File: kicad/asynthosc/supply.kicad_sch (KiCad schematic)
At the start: 52 parts, among them J1 USB_B_Micro, J17 Conn_01x02, J2 Conn_02x05_Odd_Even, U1 LM1117S-3.3, U2 LMR62421XMF, U3 USBLC6-2SC6, U4 LM1117S-5.0, U5 Si1869DH

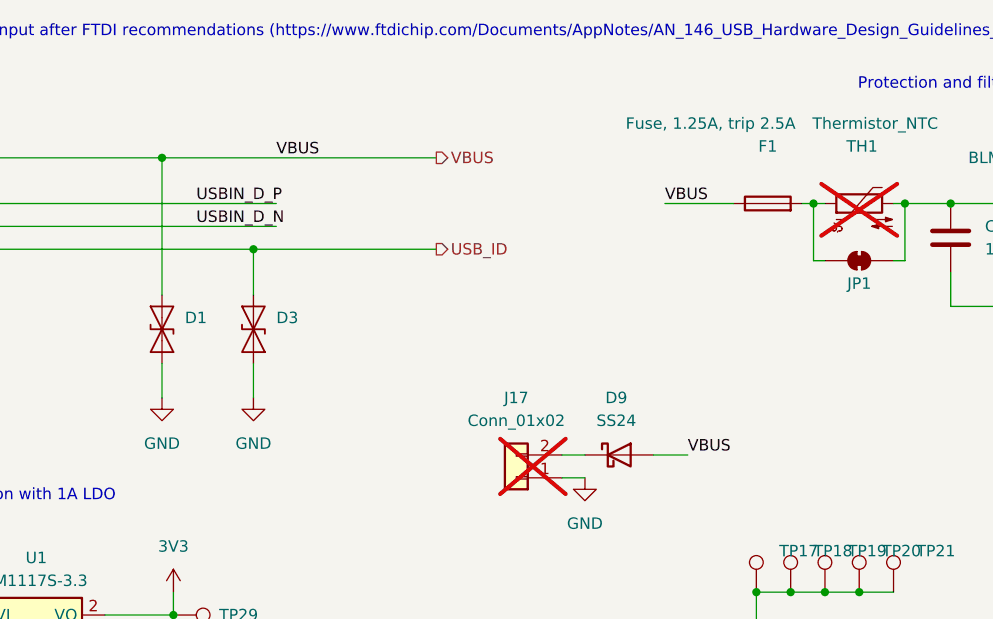
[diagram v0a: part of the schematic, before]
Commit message: fix: put all components after fuse
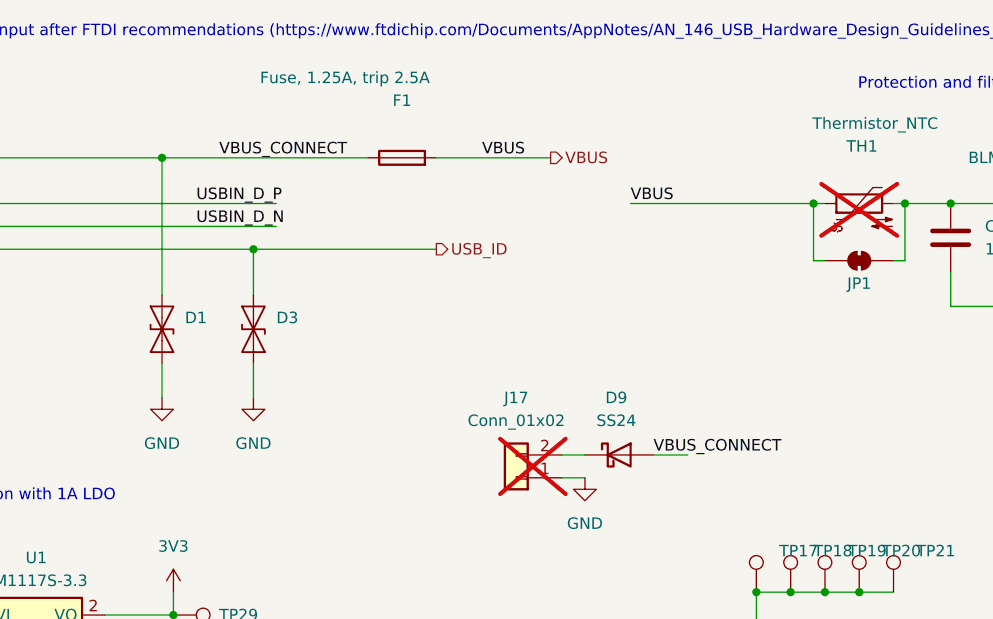
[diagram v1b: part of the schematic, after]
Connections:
- net VBUS: now also F1.2, JP1.1 (A), TH1.1; no longer D1.2 (A2), D9.2 (A), F1.1, J1.1 (VBUS)
- new net VBUS_CONNECT: D1.2 (A2), D9.2 (A), F1.1, J1.1 (VBUS)
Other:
- moved on the sheet: F1
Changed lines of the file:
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@@
 	(wire
 		(pts
-			(xy 123.19 43.18) (xy 130.81 43.18)
+			(xy 119.38 43.18) (xy 139.7 43.18)
 		)
 		(stroke
@@
 	(wire
 		(pts
-			(xy 67.31 38.1) (xy 97.79 38.1)
+			(xy 67.31 38.1) (xy 90.17 38.1)
 		)
 		(stroke
@@
 	(wire
 		(pts
+			(xy 97.79 38.1) (xy 110.49 38.1)
+		)
+		(stroke
+			(width 0)
+			(type default)
+		)
+	)
+	(wire
+		(pts
 			(xy 139.7 43.18) (xy 140.97 43.18)
 		)
@@
 	(wire
 		(pts
-			(xy 138.43 43.18) (xy 139.7 43.18)
-		)
-		(stroke
-			(width 0)
-			(type default)
-		)
-	)
-	(wire
-		(pts
 			(xy 69.85 193.04) (xy 69.85 203.2)
 		)
@@
 	)
 	(label "VBUS"
-		(at 125.73 71.12 0)
+		(at 29.21 177.8 0)
 		(fields_autoplaced yes)
 		(effects
@@
 		)
 	)
-	(label "VBUS"
-		(at 29.21 177.8 0)
+	(label "VBUS_CONNECT"
+		(at 73.66 38.1 0)
 		(fields_autoplaced yes)
 		(effects
@@
 		)
 	)
+	(label "VBUS_CONNECT"
+		(at 121.92 71.12 0)
+		(fields_autoplaced yes)
+		(effects
+			(font
+				(size 1.27 1.27)
+			)
+			(justify left bottom)
+		)
+	)
 	(label "5V_EUR"
 		(at 120.65 248.92 0)
@@
 	)
 	(label "VBUS"
-		(at 123.19 43.18 0)
+		(at 119.38 43.18 0)
 		(fields_autoplaced yes)
 		(effects
@@
 	)
 	(label "VBUS"
-		(at 80.01 38.1 0)
+		(at 102.87 38.1 0)
 		(fields_autoplaced yes)
 		(effects
@@
 	(hierarchical_label "VBUS"
 		(shape output)
-		(at 97.79 38.1 0)
+		(at 110.49 38.1 0)
 		(fields_autoplaced yes)
 		(effects
@@
 	(symbol
 		(lib_id "Device:Fuse")
-		(at 134.62 43.18 90)
+		(at 93.98 38.1 90)
 		(unit 1)
 		(exclude_from_sim yes)
@@
 		(dnp no)
 		(property "Reference" "F1"
-			(at 134.62 36.83 90)
+			(at 93.98 31.75 90)
 			(effects
 				(font
@@
 		)
 		(property "Value" "Fuse, 1.25A, trip 2.5A"
-			(at 128.27 34.29 90)
+			(at 87.63 29.21 90)
 			(effects
 				(font
@@
 		)
 		(property "Footprint" "Resistor_SMD:R_0805_2012Metric"
-			(at 134.62 44.958 90)
+			(at 93.98 39.878 90)
 			(effects
 				(font
@@
 		)
 		(property "Datasheet" "~"
-			(at 134.62 43.18 0)
+			(at 93.98 38.1 0)
 			(effects
 				(font
@@
 		)
 		(property "Description" "Fuse"
-			(at 134.62 43.18 0)
+			(at 93.98 38.1 0)
 			(effects
 				(font
@@
 		)
 		(property "RefNum" "_generic_"
-			(at 134.62 43.18 90)
+			(at 93.98 38.1 90)
 			(effects
 				(font
@@
 		)
 		(property "LCSC" ""
-			(at 134.62 43.18 0)
+			(at 93.98 38.1 0)
 			(effects
 				(font
@@
 		)
 		(property "Manufacturer" ""
-			(at 134.62 43.18 0)
+			(at 93.98 38.1 0)
 			(effects
 				(font
@@
 		)
 		(property "JLC" "0805"
-			(at 134.62 43.18 0)
+			(at 93.98 38.1 0)
 			(effects
 				(font

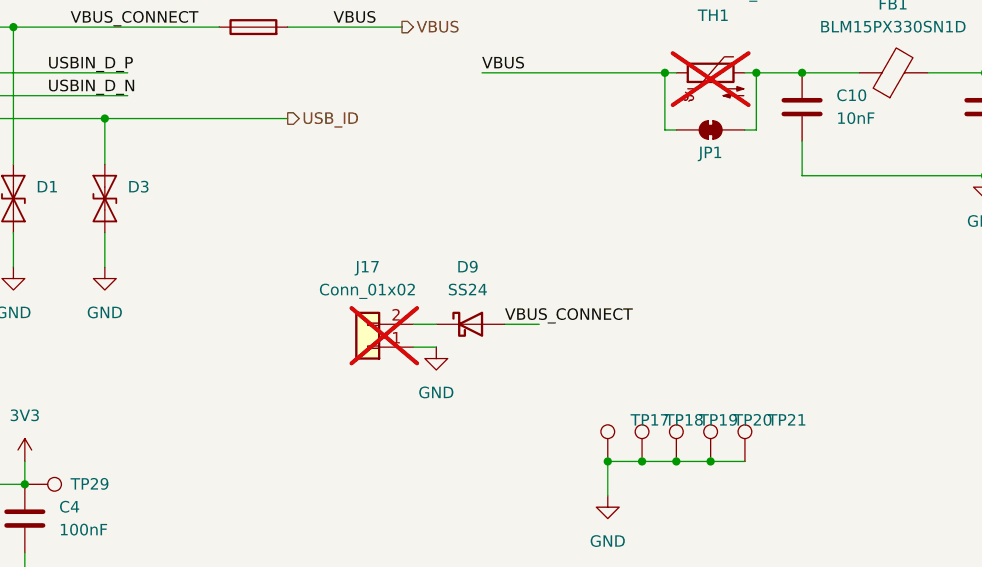
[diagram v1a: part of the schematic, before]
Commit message: fix: divider bridge stupid mistake
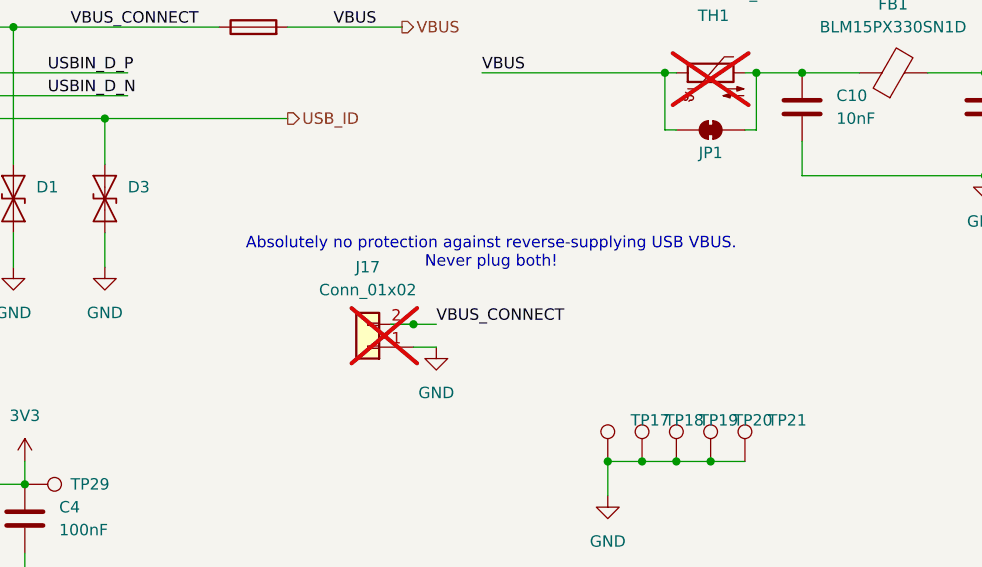
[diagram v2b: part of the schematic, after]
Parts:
- removed D9: SS24, Diode_SMD:D_SMA, symbol Diode:SS24
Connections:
- net VBUS_CONNECT: now also J17.2 (Pin_2)
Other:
- note added: "Absolutely no protection against reverse-supplying USB VBUS. Never plug both!"
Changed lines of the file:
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@@
 	)
 	(junction
+		(at 111.76 71.12)
+		(diameter 0)
+		(color 0 0 0 0)
+	)
+	(junction
 		(at 91.44 193.04)
 		(diameter 0)
@@
 	(wire
 		(pts
-			(xy 111.76 71.12) (xy 114.3 71.12)
+			(xy 109.22 71.12) (xy 111.76 71.12)
 		)
 		(stroke
@@
 	(wire
 		(pts
-			(xy 125.73 71.12) (xy 121.92 71.12)
-		)
-		(stroke
-			(width 0)
-			(type default)
-		)
-	)
-	(wire
-		(pts
 			(xy 91.44 203.2) (xy 91.44 209.55)
 		)
@@
 	(wire
 		(pts
+			(xy 111.76 71.12) (xy 114.3 71.12)
+		)
+		(stroke
+			(width 0)
+			(type default)
+		)
+	)
+	(wire
+		(pts
 			(xy 52.07 187.96) (xy 46.99 187.96)
 		)
@@
 		)
 	)
+	(text "Absolutely no protection against reverse-supplying USB VBUS.\nNever plug both!"
+		(exclude_from_sim no)
+		(at 120.396 63.246 0)
+		(effects
+			(font
+				(size 1.27 1.27)
+			)
+		)
+	)
 	(text "Display supply for standalone Eurorack"
 		(exclude_from_sim no)
@@
 	)
 	(label "VBUS_CONNECT"
-		(at 121.92 71.12 0)
+		(at 114.3 71.12 0)
 		(fields_autoplaced yes)
 		(effects
@@
 					(unit 1)
 				)
-			)
-		)
-	)
-	(symbol
-		(lib_id "Diode:SS24")
-		(at 118.11 71.12 0)
-		(unit 1)
-		(exclude_from_sim no)
-		(in_bom yes)
-		(on_board yes)
-		(dnp no)
-		(fields_autoplaced yes)
-		(property "Reference" "D9"
-			(at 117.7925 64.77 0)
-			(effects
-				(font
-					(size 1.27 1.27)
-				)
-			)
-		)
-		(property "Value" "SS24"
-			(at 117.7925 67.31 0)
-			(effects
-				(font
-					(size 1.27 1.27)
-				)
-			)
-		)
-		(property "Footprint" "Diode_SMD:D_SMA"
-			(at 118.11 75.565 0)
-			(effects
-				(font
-					(size 1.27 1.27)
-				)
-				(hide yes)
-			)
-		)
-		(property "Datasheet" "https://www.vishay.com/docs/88748/ss22.pdf"
-			(at 118.11 71.12 0)
-			(effects
-				(font
-					(size 1.27 1.27)
-				)
-				(hide yes)
-			)
-		)
-		(property "Description" "40V 2A Schottky Diode, SMA"
-			(at 118.11 71.12 0)
-			(effects
-				(font
-					(size 1.27 1.27)
-				)
-				(hide yes)
-			)
-		)
-		(property "LCSC" "C3014007"
-			(at 118.11 71.12 0)
-			(effects
-				(font
-					(size 1.27 1.27)
-				)
-				(hide yes)
-			)
-		)
-		(property "Manufacturer" "Fosan"
-			(at 118.11 71.12 0)
-			(effects
-				(font
-					(size 1.27 1.27)
-				)
-				(hide yes)
-			)
-		)
-		(property "RefNum" "SS24"
-			(at 118.11 71.12 0)
-			(effects
-				(font
-					(size 1.27 1.27)
-				)
-				(hide yes)
-			)
-		)
-		(property "JLC" "SMA"
-			(at 118.11 71.12 0)
-			(effects
-				(font
-					(size 1.27 1.27)
-				)
-				(hide yes)
-			)
-		)
-		(pin "1"
-		)
-		(pin "2"
-		)
-		(instances
-			(project "asynthosc"
-				(path "/d73e377a-a016-415f-8824-91cc6e4907b9/22ca5166-338c-4a24-8f8a-545e4a0286bf"
-					(reference "D9")
-					(unit 1)
-				)

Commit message: fix: ldo tab is vout
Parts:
- U1, U4: footprint Package_TO_SOT_SMD:SOT-223 -> Package_TO_SOT_SMD:SOT-223-3_TabPin2
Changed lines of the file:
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@@
 			)
 		)
-		(property "Footprint" "Package_TO_SOT_SMD:SOT-223"
+		(property "Footprint" "Package_TO_SOT_SMD:SOT-223-3_TabPin2"
 			(at 105.41 255.27 0)
 			(effects
@@
 			)
 		)
-		(property "Footprint" "Package_TO_SOT_SMD:SOT-223"
+		(property "Footprint" "Package_TO_SOT_SMD:SOT-223-3_TabPin2"
 			(at 53.34 88.9 0)
 			(effects

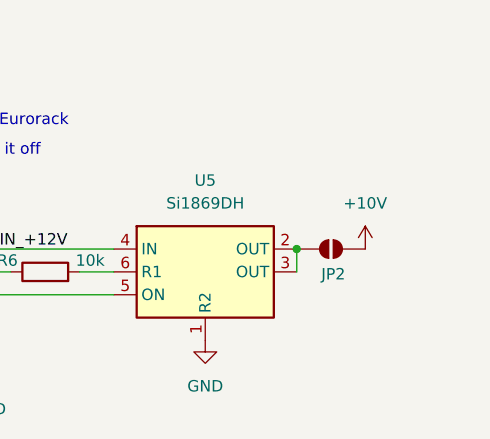
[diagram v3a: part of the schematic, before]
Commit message: sch: add decoupling capacitor to 10V switch
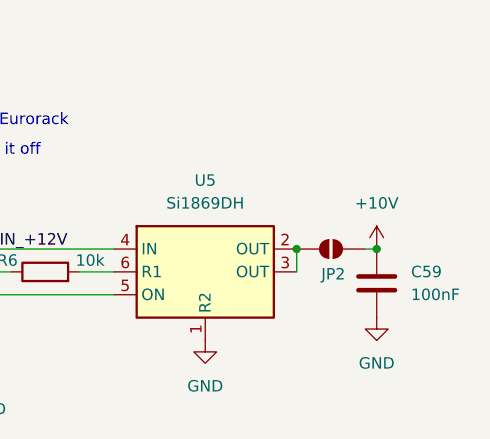
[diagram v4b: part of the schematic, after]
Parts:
- added C59: 100nF, Capacitor_SMD:C_0805_2012Metric, symbol Device:C
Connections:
- net +10V: now also C59.1
- net GND: now also C59.2
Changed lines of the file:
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@@
 	)
 	(junction
+		(at 219.71 255.27)
+		(diameter 0)
+		(color 0 0 0 0)
+	)
+	(junction
 		(at 154.94 43.18)
 		(diameter 0)
@@
 	(wire
 		(pts
+			(xy 219.71 255.27) (xy 218.44 255.27)
+		)
+		(stroke
+			(width 0)
+			(type default)
+		)
+	)
+	(wire
+		(pts
 			(xy 97.79 38.1) (xy 110.49 38.1)
 		)
@@
 	)
 	(symbol
+		(lib_id "Device:C")
+		(at 219.71 259.08 0)
+		(unit 1)
+		(exclude_from_sim no)
+		(in_bom yes)
+		(on_board yes)
+		(dnp no)
+		(fields_autoplaced yes)
+		(property "Reference" "C59"
+			(at 223.52 257.8099 0)
+			(effects
+				(font
+					(size 1.27 1.27)
+				)
+				(justify left)
+			)
+		)
+		(property "Value" "100nF"
+			(at 223.52 260.3499 0)
+			(effects
+				(font
+					(size 1.27 1.27)
+				)
+				(justify left)
+			)
+		)
+		(property "Footprint" "Capacitor_SMD:C_0805_2012Metric"
+			(at 220.6752 262.89 0)
+			(effects
+				(font
+					(size 1.27 1.27)
+				)
+				(hide yes)
+			)
+		)
+		(property "Datasheet" "~"
+			(at 219.71 259.08 0)
+			(effects
+				(font
+					(size 1.27 1.27)
+				)
+				(hide yes)
+			)
+		)
+		(property "Description" "Unpolarized capacitor"
+			(at 219.71 259.08 0)
+			(effects
+				(font
+					(size 1.27 1.27)
+				)
+				(hide yes)
+			)
+		)
+		(property "LCSC" ""
+			(at 219.71 259.08 0)
+			(effects
+				(font
+					(size 1.27 1.27)
+				)
+				(hide yes)
+			)
+		)
+		(property "Manufacturer" ""
+			(at 219.71 259.08 0)
+			(effects
+				(font
+					(size 1.27 1.27)
+				)
+				(hide yes)
+			)
+		)
+		(property "RefNum" "_generic_"
+			(at 219.71 259.08 0)
+			(effects
+				(font
+					(size 1.27 1.27)
+				)
+				(hide yes)
+			)
+		)
+		(property "JLC" "0805"
+			(at 219.71 259.08 0)
+			(effects
+				(font
+					(size 1.27 1.27)
+				)
+				(hide yes)
+			)
+		)
+		(pin "2"
+		)
+		(pin "1"
+		)
+		(instances
+			(project "asynthosc"
+				(path "/d73e377a-a016-415f-8824-91cc6e4907b9/22ca5166-338c-4a24-8f8a-545e4a0286bf"
+					(reference "C59")
+					(unit 1)
+				)
+			)
+		)
+	)
+	(symbol
 		(lib_id "Jumper:SolderJumper_2_Bridged")
 		(at 144.78 49.53 0)
@@
 	(symbol
 		(lib_id "power:+10V")
-		(at 218.44 255.27 0)
+		(at 219.71 255.27 0)
 		(unit 1)
 		(exclude_from_sim no)
@@
 		(fields_autoplaced yes)
 		(property "Reference" "#PWR029"
-			(at 218.44 259.08 0)
+			(at 219.71 259.08 0)
 			(effects
 				(font
@@
 		)
 		(property "Value" "+10V"
-			(at 218.44 250.19 0)
+			(at 219.71 250.19 0)
 			(effects
 				(font
@@
 		)
 		(property "Footprint" ""
-			(at 218.44 255.27 0)
+			(at 219.71 255.27 0)
 			(effects
 				(font
@@
 		)
 		(property "Datasheet" ""
-			(at 218.44 255.27 0)
+			(at 219.71 255.27 0)
 			(effects
 				(font
@@
 		)
 		(property "Description" "Power symbol creates a global label with name \"+10V\""
-			(at 218.44 255.27 0)
+			(at 219.71 255.27 0)
 			(effects
 				(font
@@
 					(unit 1)
 				)
+			)
+		)
+	)
+	(symbol
+		(lib_id "power:GND")
+		(at 219.71 262.89 0)
+		(unit 1)
+		(exclude_from_sim no)
+		(in_bom yes)
+		(on_board yes)
+		(dnp no)
+		(fields_autoplaced yes)
+		(property "Reference" "#PWR0161"
+			(at 219.71 269.24 0)
+			(effects
+				(font
+					(size 1.27 1.27)
+				)
+				(hide yes)
+			)
+		)
+		(property "Value" "GND"
+			(at 219.71 267.97 0)
+			(effects
+				(font
+					(size 1.27 1.27)
+				)
+			)
+		)
+		(property "Footprint" ""
+			(at 219.71 262.89 0)
+			(effects
+				(font
+					(size 1.27 1.27)
+				)
+				(hide yes)
+			)
+		)
+		(property "Datasheet" ""
+			(at 219.71 262.89 0)
+			(effects
+				(font
+					(size 1.27 1.27)
+				)
+				(hide yes)
+			)
+		)
+		(property "Description" "Power symbol creates a global label with name \"GND\" , ground"
+			(at 219.71 262.89 0)
+			(effects
+				(font
+					(size 1.27 1.27)
+				)
+				(hide yes)
+			)
+		)
+		(pin "1"
+		)
+		(instances
+			(project "asynthosc"
+				(path "/d73e377a-a016-415f-8824-91cc6e4907b9/22ca5166-338c-4a24-8f8a-545e4a0286bf"
+					(reference "#PWR0161")
+					(unit 1)
+				)

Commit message: sch: modifs on supply
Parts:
- C59: footprint Capacitor_SMD:C_0805_2012Metric -> Capacitor_SMD:C_0402_1005Metric; JLC 0805 -> 0402
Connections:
- net +10V: no longer C59.1
- net at JP2.1 (A), U5.2 (OUT), U5.3 (OUT): now also C59.1
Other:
- moved on the sheet: C59, JP2
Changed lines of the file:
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@@
 	)
 	(junction
+		(at 213.36 257.81)
+		(diameter 0)
+		(color 0 0 0 0)
+	)
+	(junction
 		(at 62.23 257.81)
 		(diameter 0)
@@
 	)
 	(junction
-		(at 219.71 255.27)
-		(diameter 0)
-		(color 0 0 0 0)
-	)
-	(junction
 		(at 154.94 43.18)
 		(diameter 0)
@@
 	)
 	(junction
-		(at 210.82 255.27)
+		(at 213.36 255.27)
 		(diameter 0)
 		(color 0 0 0 0)
@@
 	(wire
 		(pts
-			(xy 219.71 255.27) (xy 218.44 255.27)
+			(xy 222.25 255.27) (xy 220.98 255.27)
+		)
+		(stroke
+			(width 0)
+			(type default)
+		)
+	)
+	(wire
+		(pts
+			(xy 213.36 257.81) (xy 210.82 257.81)
 		)
 		(stroke
@@
 	(wire
 		(pts
-			(xy 210.82 255.27) (xy 210.82 257.81)
+			(xy 213.36 255.27) (xy 213.36 257.81)
 		)
 		(stroke
@@
 	(wire
 		(pts
+			(xy 213.36 255.27) (xy 210.82 255.27)
+		)
+		(stroke
+			(width 0)
+			(type default)
+		)
+	)
+	(wire
+		(pts
 			(xy 36.83 248.92) (xy 36.83 252.73)
 		)
@@
 	(symbol
 		(lib_id "Jumper:SolderJumper_2_Open")
-		(at 214.63 255.27 0)
+		(at 217.17 255.27 0)
 		(unit 1)
 		(exclude_from_sim yes)
@@
 		(dnp no)
 		(property "Reference" "JP2"
-			(at 214.884 258.064 0)
+			(at 217.424 258.064 0)
 			(effects
 				(font
@@
 		)
 		(property "Value" "SolderJumper_2_Open"
-			(at 214.63 251.46 0)
+			(at 217.17 251.46 0)
 			(effects
 				(font
@@
 		)
 		(property "Footprint" "Resistor_SMD:R_0402_1005Metric"
-			(at 214.63 255.27 0)
+			(at 217.17 255.27 0)
 			(effects
 				(font
@@
 		)
 		(property "Datasheet" "~"
-			(at 214.63 255.27 0)
+			(at 217.17 255.27 0)
 			(effects
 				(font
@@
 		)
 		(property "Description" "Solder Jumper, 2-pole, open"
-			(at 214.63 255.27 0)
+			(at 217.17 255.27 0)
 			(effects
 				(font
@@
 		)
 		(property "LCSC" ""
-			(at 214.63 255.27 0)
+			(at 217.17 255.27 0)
 			(effects
 				(font
@@
 		)
 		(property "Manufacturer" ""
-			(at 214.63 255.27 0)
+			(at 217.17 255.27 0)
 			(effects
 				(font
@@
 		)
 		(property "RefNum" "_na_"
-			(at 214.63 255.27 0)
+			(at 217.17 255.27 0)
 			(effects
 				(font
@@
 		)
 		(property "JLC" ""
-			(at 214.63 255.27 0)
+			(at 217.17 255.27 0)
 			(effects
 				(font
@@
 	(symbol
 		(lib_id "Device:C")
-		(at 219.71 259.08 0)
+		(at 213.36 261.62 0)
 		(unit 1)
 		(exclude_from_sim no)
@@
 		(fields_autoplaced yes)
 		(property "Reference" "C59"
-			(at 223.52 257.8099 0)
+			(at 217.17 260.3499 0)
 			(effects
 				(font
@@
 		)
 		(property "Value" "100nF"
-			(at 223.52 260.3499 0)
+			(at 217.17 262.8899 0)
 			(effects
 				(font
@@
 			)
 		)
-		(property "Footprint" "Capacitor_SMD:C_0805_2012Metric"
-			(at 220.6752 262.89 0)
+		(property "Footprint" "Capacitor_SMD:C_0402_1005Metric"
+			(at 214.3252 265.43 0)
 			(effects
 				(font
@@
 		)
 		(property "Datasheet" "~"
-			(at 219.71 259.08 0)
+			(at 213.36 261.62 0)
 			(effects
 				(font
@@
 		)
 		(property "Description" "Unpolarized capacitor"
-			(at 219.71 259.08 0)
+			(at 213.36 261.62 0)
 			(effects
 				(font
@@
 		)
 		(property "LCSC" ""
-			(at 219.71 259.08 0)
+			(at 213.36 261.62 0)
 			(effects
 				(font
@@
 		)
 		(property "Manufacturer" ""
-			(at 219.71 259.08 0)
+			(at 213.36 261.62 0)
 			(effects
 				(font
@@
 		)
 		(property "RefNum" "_generic_"
-			(at 219.71 259.08 0)
+			(at 213.36 261.62 0)
 			(effects
 				(font
@@
 			)
 		)
-		(property "JLC" "0805"
-			(at 219.71 259.08 0)
+		(property "JLC" "0402"
+			(at 213.36 261.62 0)
 			(effects
 				(font
@@
 	(symbol
 		(lib_id "power:+10V")
-		(at 219.71 255.27 0)
+		(at 222.25 255.27 0)
 		(unit 1)
 		(exclude_from_sim no)
@@
 		(fields_autoplaced yes)
 		(property "Reference" "#PWR029"
-			(at 219.71 259.08 0)
+			(at 222.25 259.08 0)
 			(effects
 				(font
@@
 		)
 		(property "Value" "+10V"
-			(at 219.71 250.19 0)
+			(at 222.25 250.19 0)
 			(effects
 				(font
@@
 		)
 		(property "Footprint" ""
-			(at 219.71 255.27 0)
+			(at 222.25 255.27 0)
 			(effects
 				(font
@@
 		)
 		(property "Datasheet" ""
-			(at 219.71 255.27 0)
+			(at 222.25 255.27 0)
 			(effects
 				(font
@@
 		)
 		(property "Description" "Power symbol creates a global label with name \"+10V\""
-			(at 219.71 255.27 0)
+			(at 222.25 255.27 0)
 			(effects
 				(font
@@
 	(symbol
 		(lib_id "power:GND")
-		(at 219.71 262.89 0)
+		(at 213.36 265.43 0)
 		(unit 1)
 		(exclude_from_sim no)
@@
 		(fields_autoplaced yes)
 		(property "Reference" "#PWR0161"
-			(at 219.71 269.24 0)
+			(at 213.36 271.78 0)
 			(effects
 				(font
@@
 		)
 		(property "Value" "GND"
-			(at 219.71 267.97 0)
+			(at 213.36 270.51 0)
 			(effects
 				(font
@@
 		)
 		(property "Footprint" ""
-			(at 219.71 262.89 0)
+			(at 213.36 265.43 0)
 			(effects
 				(font
@@
 		)
 		(property "Datasheet" ""
-			(at 219.71 262.89 0)
+			(at 213.36 265.43 0)
 			(effects
 				(font
@@
 		)
 		(property "Description" "Power symbol creates a global label with name \"GND\" , ground"
-			(at 219.71 262.89 0)
+			(at 213.36 265.43 0)
 			(effects
 				(font
